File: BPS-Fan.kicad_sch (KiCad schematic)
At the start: 45 parts, among them J1 LDRBRDConn, J10 FAN9, J11 FAN10, J12 FAN11, J13 FAN12, J2 FAN1, J3 FAN2, J4 FAN3, J5 FAN4, J6 FAN5, J7 FAN6, J8 FAN7, J9 FAN8, Q1 BUK9M34-100EX, Q10 BUK9M34-100EX, Q11 BUK9M34-100EX, Q12 BUK9M34-100EX, Q2 BUK9M34-100EX, Q3 BUK9M34-100EX, Q4 BUK9M34-100EX, Q5 BUK9M34-100EX, Q6 BUK9M34-100EX, Q7 BUK9M34-100EX, Q8 BUK9M34-100EX, Q9 BUK9M34-100EX

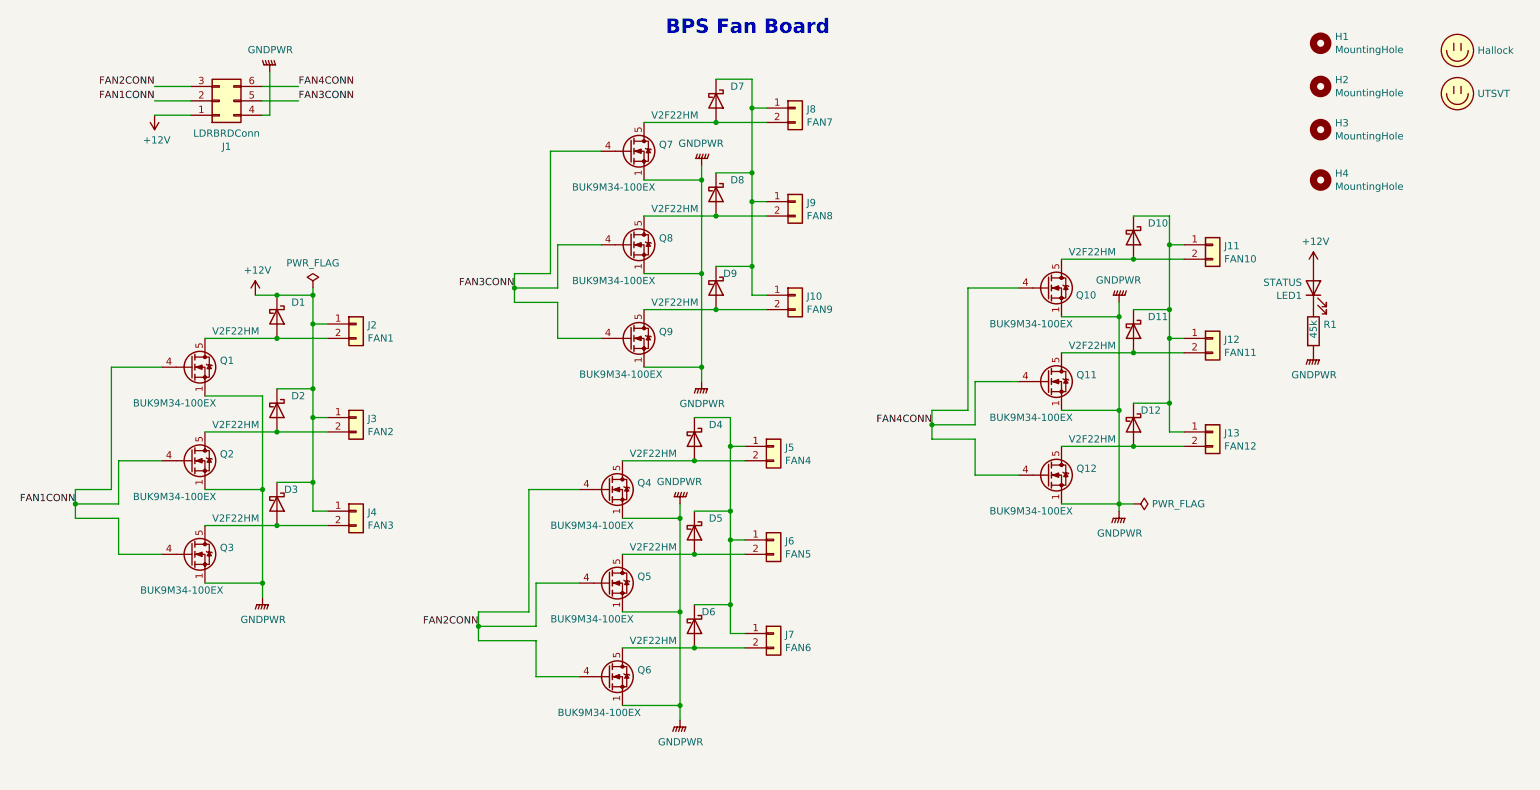
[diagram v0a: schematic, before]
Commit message: Replaced mosfet, added Hannah's changes, updated bom and data sheets
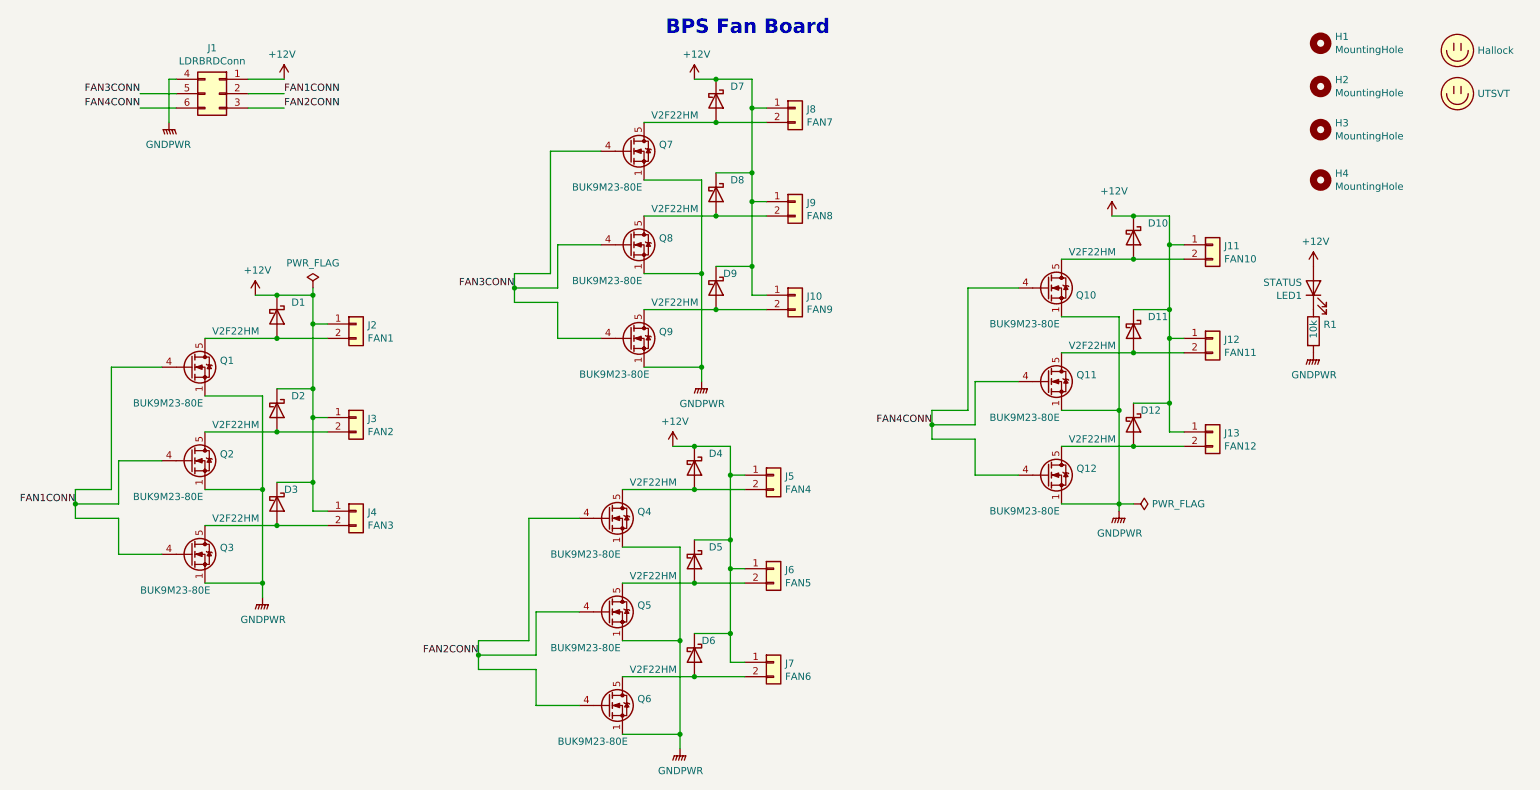
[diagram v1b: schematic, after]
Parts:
- Q1, Q10, Q11, Q12, Q2, Q3, Q4, Q5, Q6, Q7, Q8, Q9: value BUK9M34-100EX -> BUK9M23-80E; symbol Transistor_FET:BUK9M34-100EX -> Transistor_FET:BUK9M23-80EX
- R1: value 45k -> 10k
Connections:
- net +12V: now also D10.1 (K), D11.1 (K), D12.1 (K), D4.1 (K), D5.1 (K), D6.1 (K), D7.1 (K), D8.1 (K), D9.1 (K), J10.1 (Pin_1), J11.1 (Pin_1), J12.1 (Pin_1), J13.1 (Pin_1), J5.1 (Pin_1), J6.1 (Pin_1), J7.1 (Pin_1), J8.1 (Pin_1), J9.1 (Pin_1)
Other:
- moved on the sheet: D4, D5, D6, J1, J5, J6, J7, Q4, Q5, Q6

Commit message: made adjustments after looking at data sheets and realizing we only need 1 mosfet and 1 diode per 3 fans
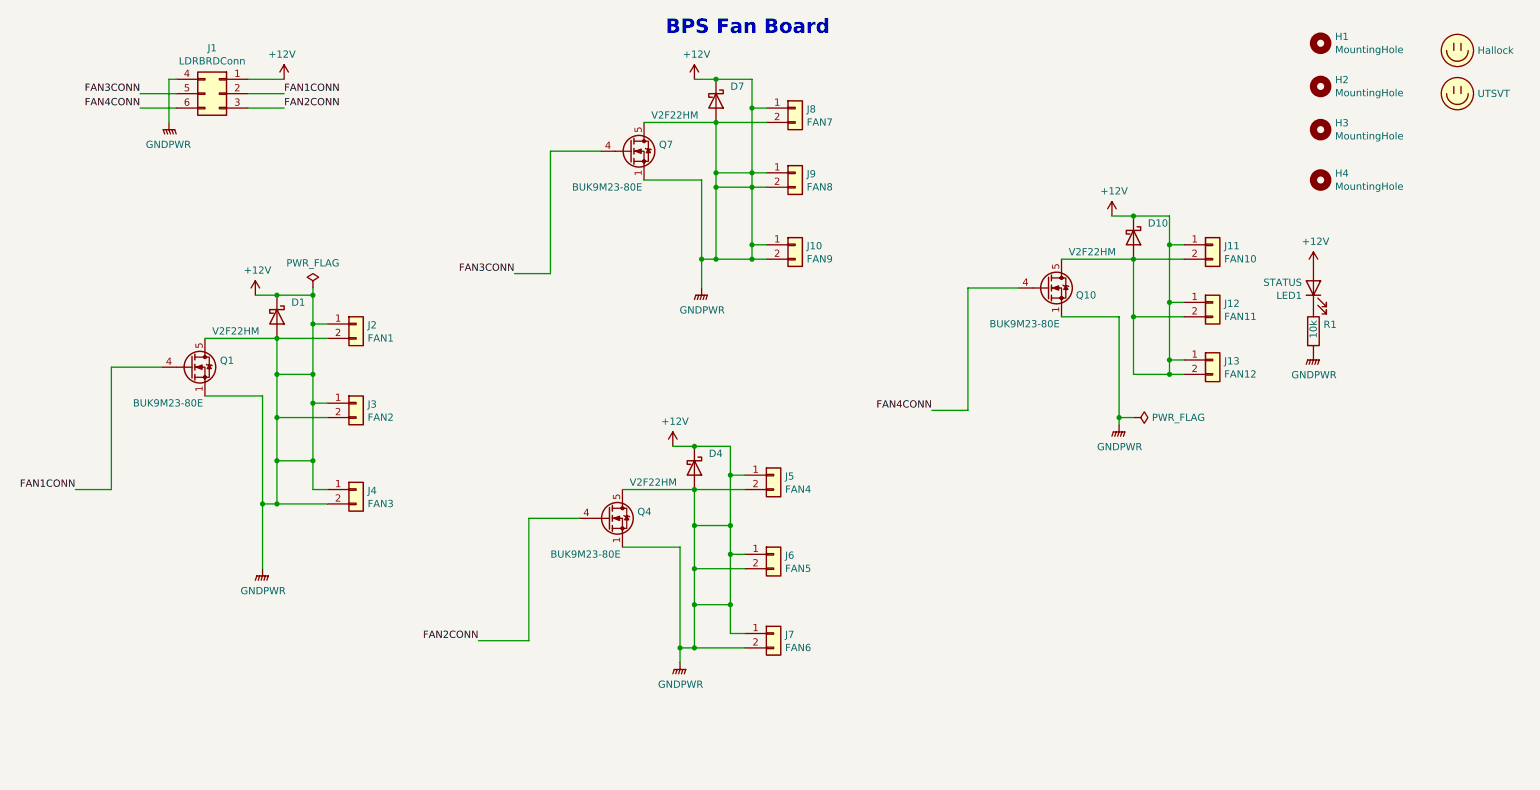
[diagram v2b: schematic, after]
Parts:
- removed D11, D12, D2, D3, D5, D6, D8, D9: V2F22HM, UTSVT_Passive:V2F22HM, symbol Diode:C3D25170H
- removed Q11, Q12, Q2, Q3, Q5, Q6, Q8, Q9: BUK9M23-80E, Package_TO_SOT_SMD:LFPAK33, symbol Transistor_FET:BUK9M23-80EX
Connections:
- net GNDPWR is gone; now on net +12V: J1.4 (Pin_4), Q1.1 (S), Q1.2 (S), Q1.3 (S), Q10.1 (S), Q10.2 (S), Q10.3 (S), Q4.1 (S), Q4.2 (S), Q4.3 (S), Q7.1 (S), Q7.2 (S), Q7.3 (S), R1.2
- net +12V: now also D1.2 (A), D10.2 (A), D4.2 (A), D7.2 (A), J10.2 (Pin_2), J11.2 (Pin_2), J12.2 (Pin_2), J13.2 (Pin_2), J2.2 (Pin_2), J3.2 (Pin_2), J4.2 (Pin_2), J5.2 (Pin_2), J6.2 (Pin_2), J7.2 (Pin_2), J8.2 (Pin_2), J9.2 (Pin_2), Q1.5 (D), Q10.5 (D), Q4.5 (D), Q7.5 (D)
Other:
- moved on the sheet: J10, J12, J13, J3, J4, J6, J7, J9
